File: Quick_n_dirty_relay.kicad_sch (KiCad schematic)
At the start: 10 parts, among them J6 Conn_01x03_Pin, Q12 MMBT5551 200-300, U5 LTV-217-B-G

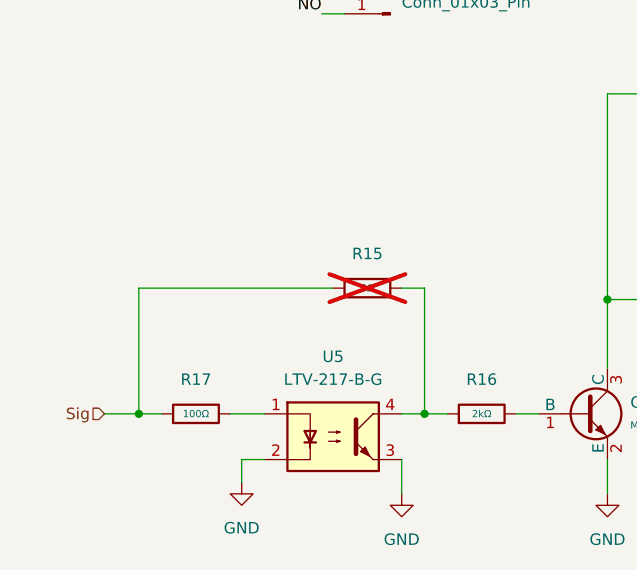
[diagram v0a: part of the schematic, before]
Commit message: fixed NPN configuration in optocoupler
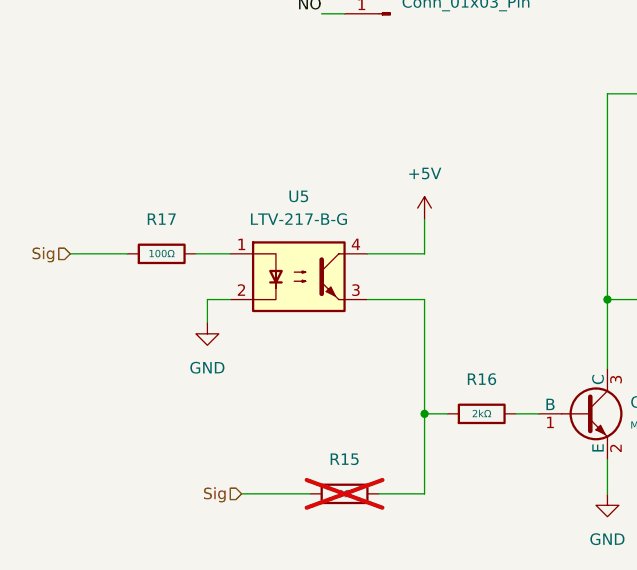
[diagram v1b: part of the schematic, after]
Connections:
- net +5V: now also U5.4
- net GND: no longer U5.3
- net at R15.2, R16.1: now also U5.3; no longer U5.4
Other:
- moved on the sheet: R17, U5

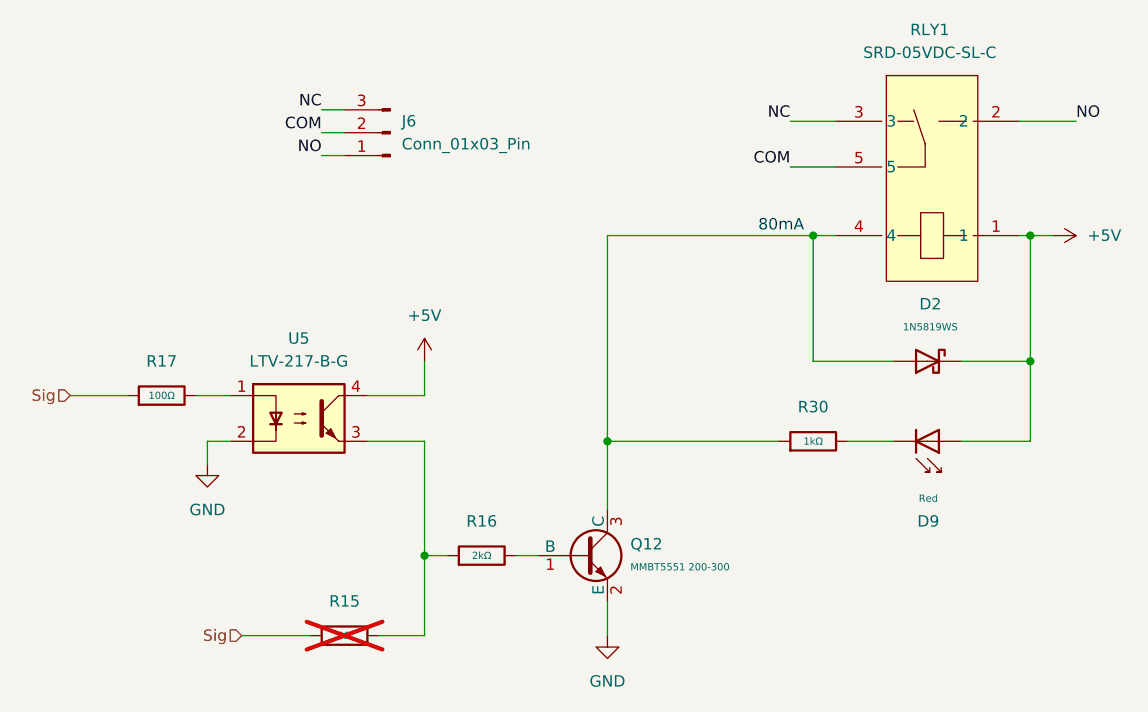
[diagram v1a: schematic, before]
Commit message: changed headers and relays to better one
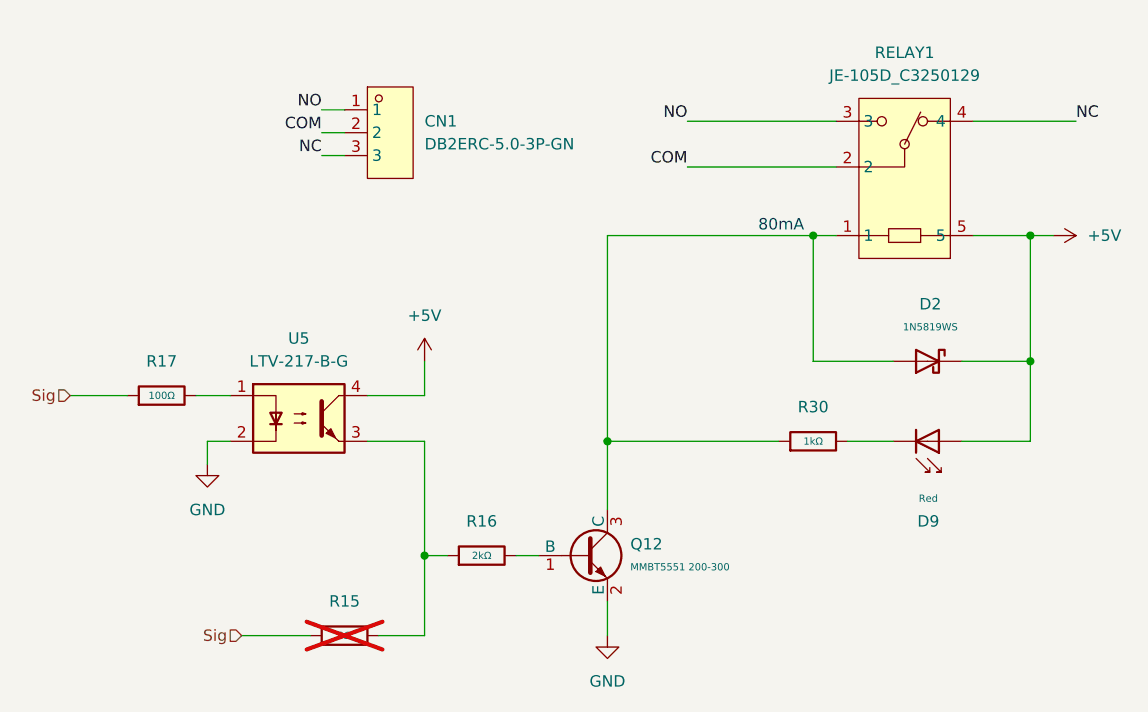
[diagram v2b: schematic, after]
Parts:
- removed J6: Conn_01x03_Pin, Connector_JST:JST_XH_S3B-XH-A_1x03_P2.50mm_Horizontal, symbol Connector:Conn_01x03_Pin
- removed RLY1: SRD-05VDC-SL-C, SRD-05VDC-SL-C:RELAY-TH_SRD-XXVDC-XL-C, symbol SRD-05VDC-SL-C:SRD-05VDC-SL-C
- added CN1: DB2ERC-5.0-3P-GN, DB2ERC-5:CONN-TH_3P-P5.00_DB2ERC-5.0-3P-GN, symbol DB2ERC-5:DB2ERC-5.0-3P-GN
- added RELAY1: JE-105D_C3250129, JE-105D_C3250129:RELAY-TH_JE-1XXD, symbol JE-105D:JE-105D_C3250129
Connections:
- net +5V: now also RELAY1.5
- net COM: now also CN1.2, RELAY1.2
- net NC: now also CN1.3, RELAY1.4
- net NO: now also CN1.1, RELAY1.3
- net at D2.2, Q12.3 (C), R30.1: now also RELAY1.1
